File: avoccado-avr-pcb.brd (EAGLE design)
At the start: 17.8 x 33 mm, 29 parts, among them IC1 MCP1703CB, Q1 #MHz, Q2 MOSFET-NCHANNEL2N7002PW, U1 ATMEGA168#, U2 MCP73831, X1 Micro USB

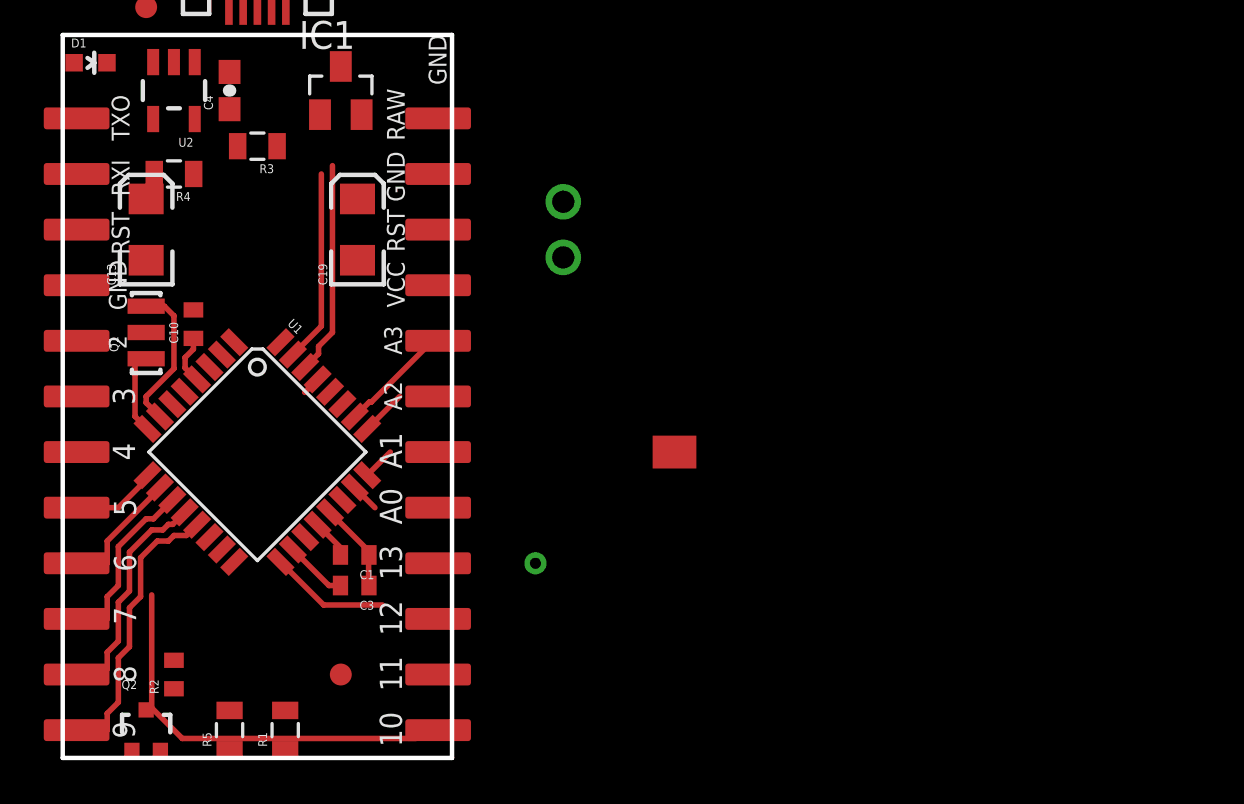
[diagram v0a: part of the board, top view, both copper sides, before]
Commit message: add NRF24 header wip
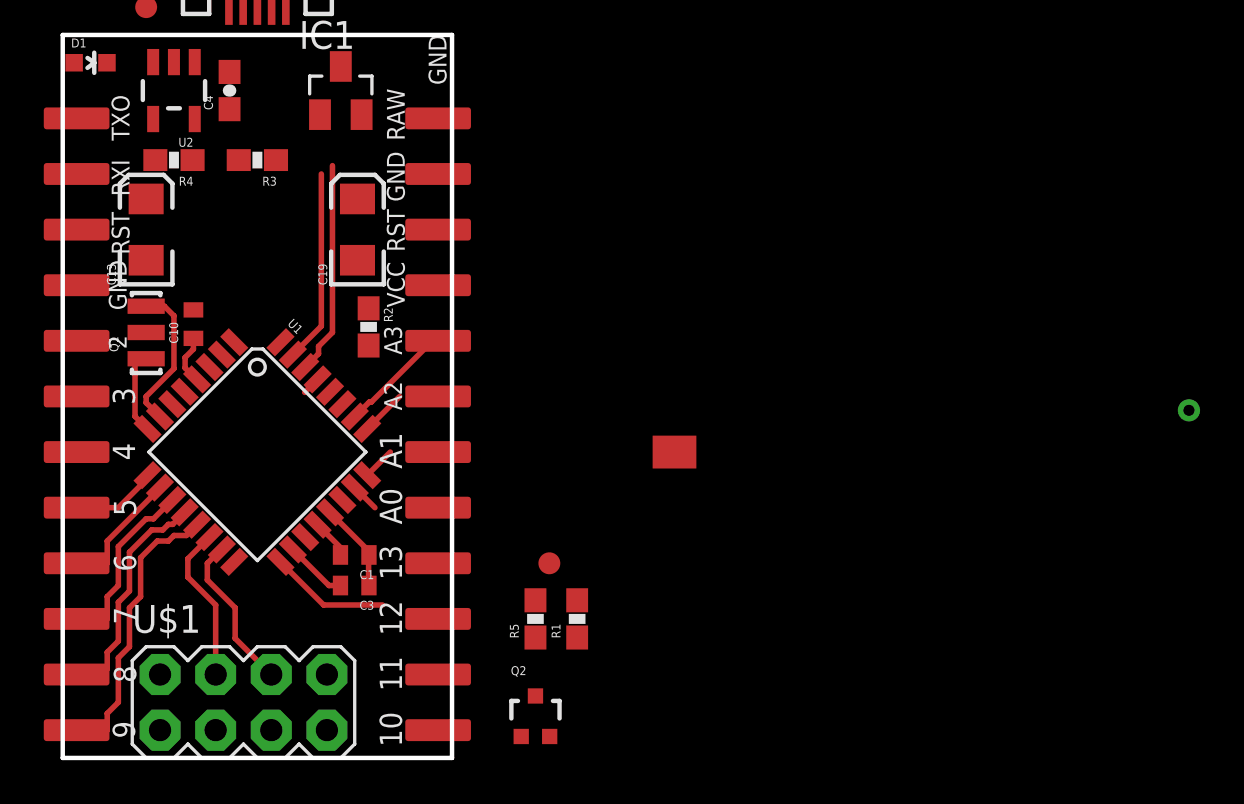
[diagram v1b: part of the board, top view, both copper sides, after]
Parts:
- removed JP2: (no value), SparkFun:1X02
- added U$1: M04X2, SparkFun-Connectors:2X4
- R1, R5: device SparkFun-Passives:0805 -> SparkFun-Resistors:0603-RES
- R2: device SparkFun:C0402 -> SparkFun-Resistors:0603-RES
- R3, R4: device SparkFun-Resistors:0805 -> SparkFun-Resistors:0603-RES
- moved R2 18.2 mm to (22.9, 31.1), turned to 270 degrees
- moved Q2 17.8 mm to (30.5, 13.3)
- moved R5 14.9 mm to (30.5, 17.8)
- moved R1 14.3 mm to (32.4, 17.8)
- moved U$2 10.8 mm to (31.1, 20.3)
- moved R3 0.63 mm to (17.8, 38.7)
- moved R4 0.63 mm to (14.0, 38.7)
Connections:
- new net 3.3V: U$1.2
- net A4: no longer JP2.1
- net A5: no longer JP2.2
- net D10: now also U$1.4
- net GND: now also U$1.1
- net MISO: now also U$1.7
- net MOSI: now also U$1.6
- net SCK: now also U$1.5
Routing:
- net D10: track 17.8 -> 7.21 mm
- net MOSI: track 0.00 -> 7.22 mm

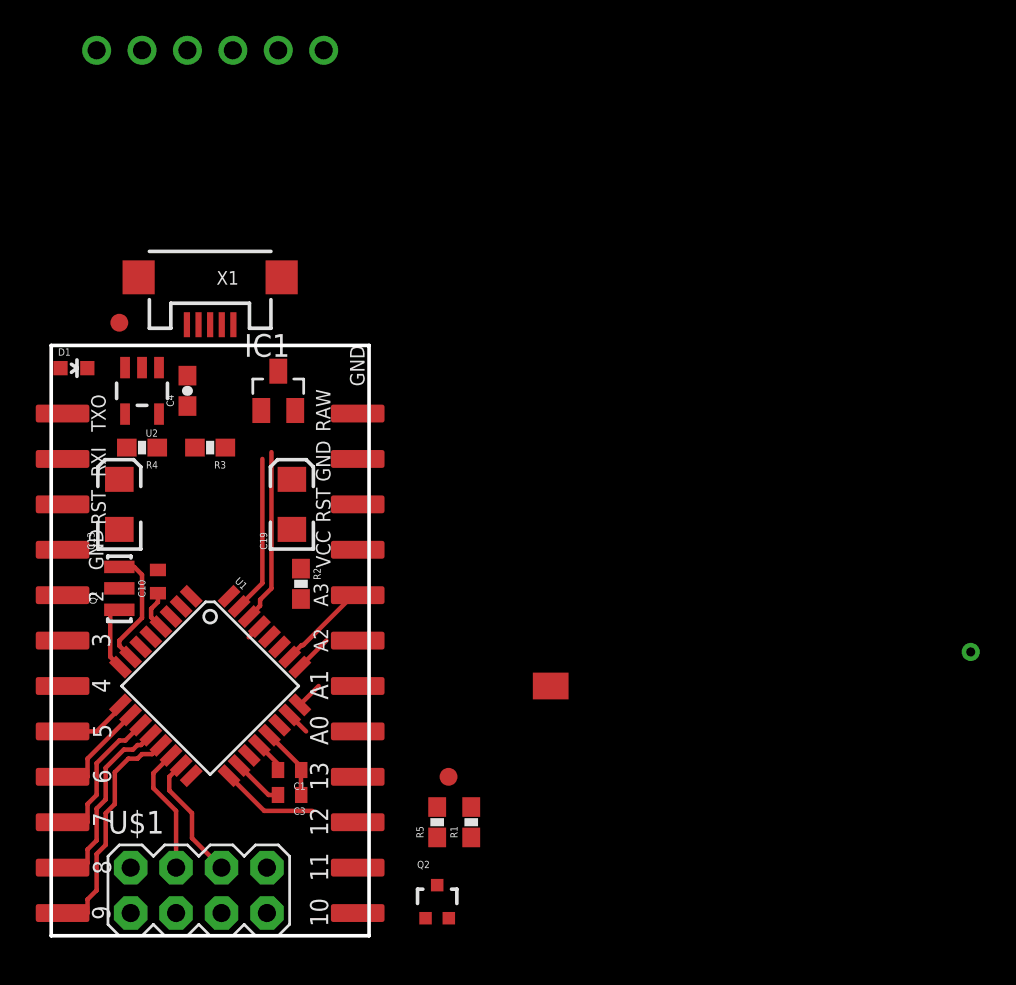
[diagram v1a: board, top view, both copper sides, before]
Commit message: reroute NRF24 header with bottom layer, add MPU6050 satellite board
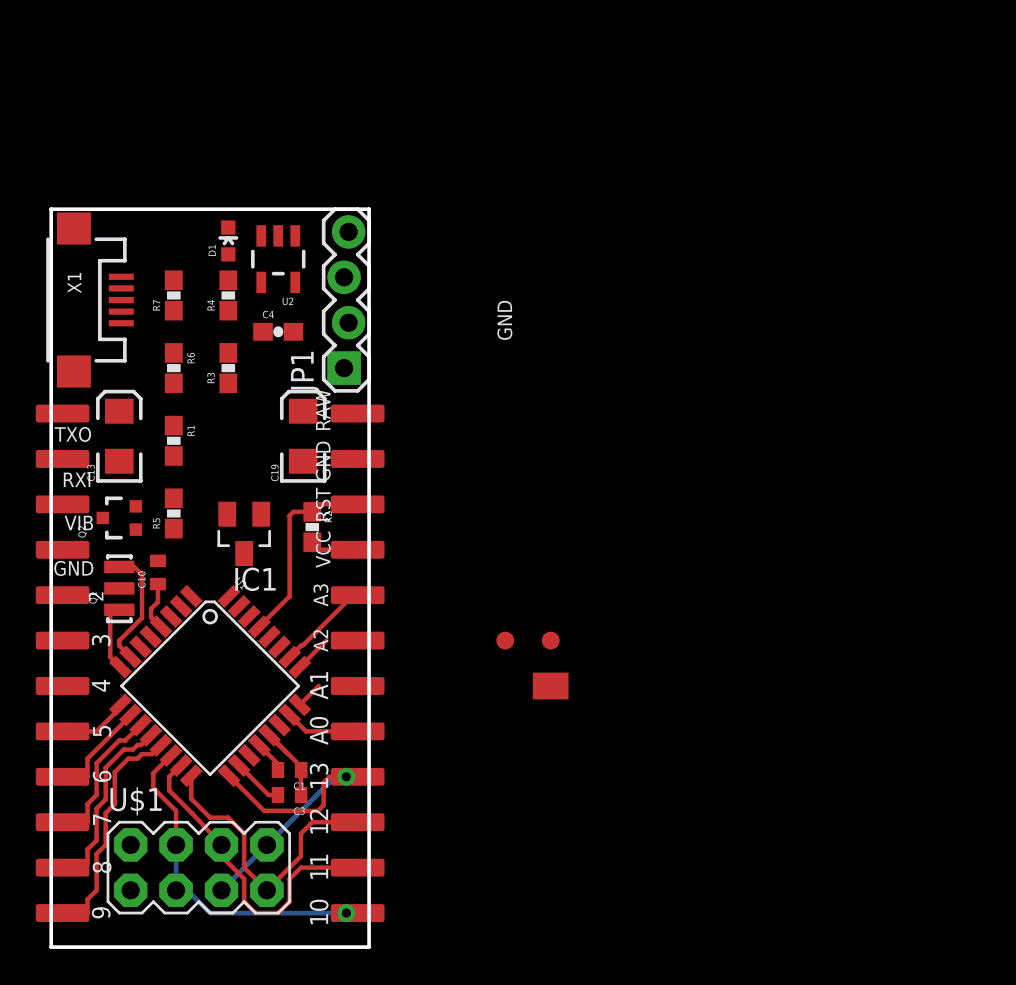
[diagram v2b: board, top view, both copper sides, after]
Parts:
- added R6, R7: 68, SparkFun-Resistors:0603-RES
- JP1: value FTDI Basic -> (none); device SparkFun:1X06 -> SparkFun-Connectors:1X04_LOCK
- moved U$4 30.0 mm to (36.8, 27.9)
- moved Q2 27.9 mm to (12.7, 34.8), turned to 90 degrees
- moved R1 27.1 mm to (15.7, 39.1), turned to 270 degrees
- moved R5 22.7 mm to (15.7, 35.1)
- moved JP1 22.6 mm to (25.4, 43.2), flipped to the top, turned to 90 degrees
- moved D1 11.2 mm to (18.8, 50.3), turned to 0 degrees
- moved U2 10.6 mm to (21.6, 49.3)
- moved R4 9.78 mm to (18.8, 47.2), turned to 90 degrees
- moved U$2 8.26 mm to (34.3, 27.9)
- moved IC1 8.22 mm to (19.7, 33.9), turned to 180 degrees
- moved X1 7.73 mm to (10.2, 47.0), turned to 270 degrees
- moved C4 6.06 mm to (21.6, 45.2), turned to 0 degrees
- moved R3 4.56 mm to (18.8, 43.2), turned to 90 degrees
- moved C19 3.86 mm to (23.0, 39.4)
- moved C13 3.81 mm to (12.7, 39.4)
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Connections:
- net RAW renamed BAT
- net VIN1 renamed BUS
- removed net DTR: JP1.1
- new net N$7: R7.1, X1.D+
- new net N$8: R6.1, X1.D-
- new net VIBR: JP11.2, Q2.3
- net A4: now also JP1.4
- net A5: now also JP1.3
- net D2: now also R7.2
- net D7: now also R6.2
- net GND: now also JP1.1; no longer JP1.5, JP1.6
- net RESET: no longer JP11.2
- net RXI: no longer JP1.3
- net TXO: no longer JP1.2
- net VCC: now also JP1.2; no longer JP1.4
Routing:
- net MISO: track 0.00 -> 16.2 mm
- net SCK: track 5.48 -> 19.2 mm, vias 0 -> 1
- net D10: track 7.21 -> 18.8 mm, vias 0 -> 1
- net MOSI: track 7.22 -> 18.0 mm
- net RESET: track 0.84 -> 11.0 mm
- net RXI: track 9.71 -> 0.00 mm
- net TXO: track 8.79 -> 0.00 mm
- net VCC: track 5.30 -> 8.39 mm
- net A0: track 1.30 -> 4.19 mm
- net GND: track 4.11 -> 4.96 mm, vias 1 -> 0
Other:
- board size 17.8 x 33 mm -> 17.8 x 41.3 mm
- board text added: "VIB"

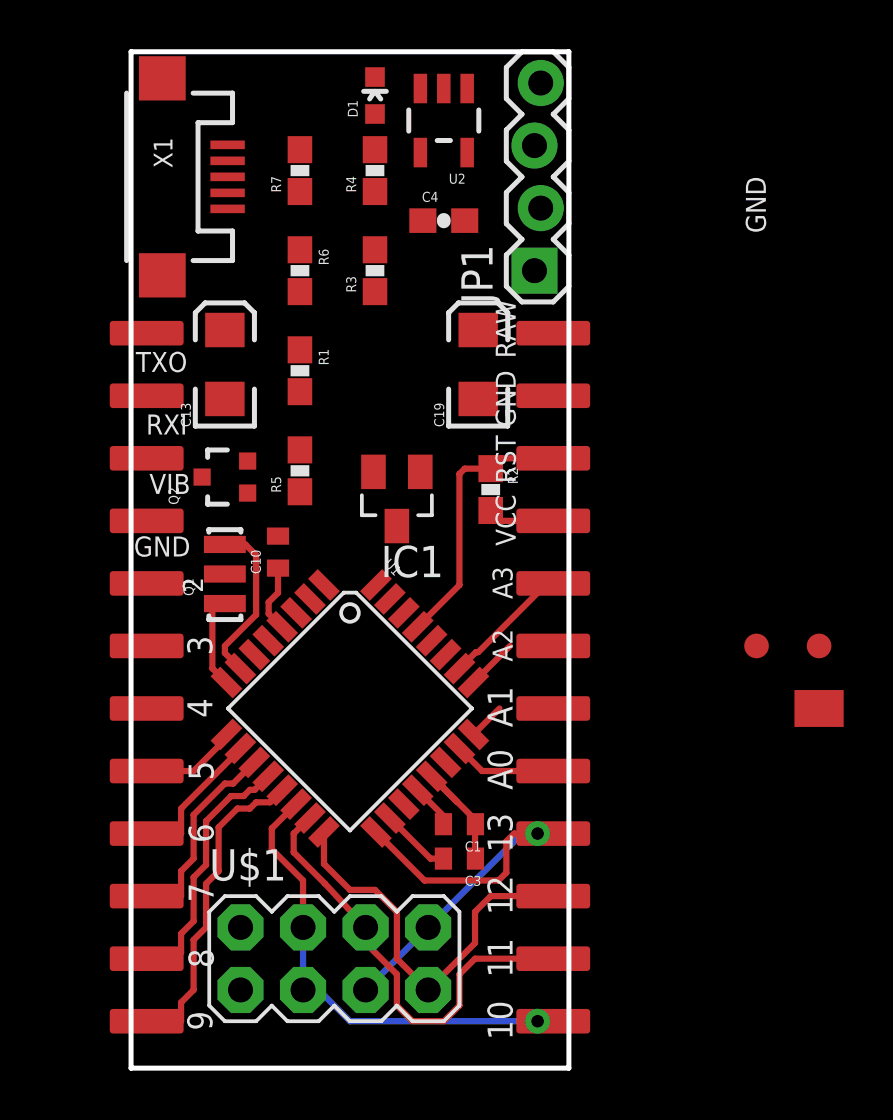
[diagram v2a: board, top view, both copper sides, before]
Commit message: route MPU6050 header
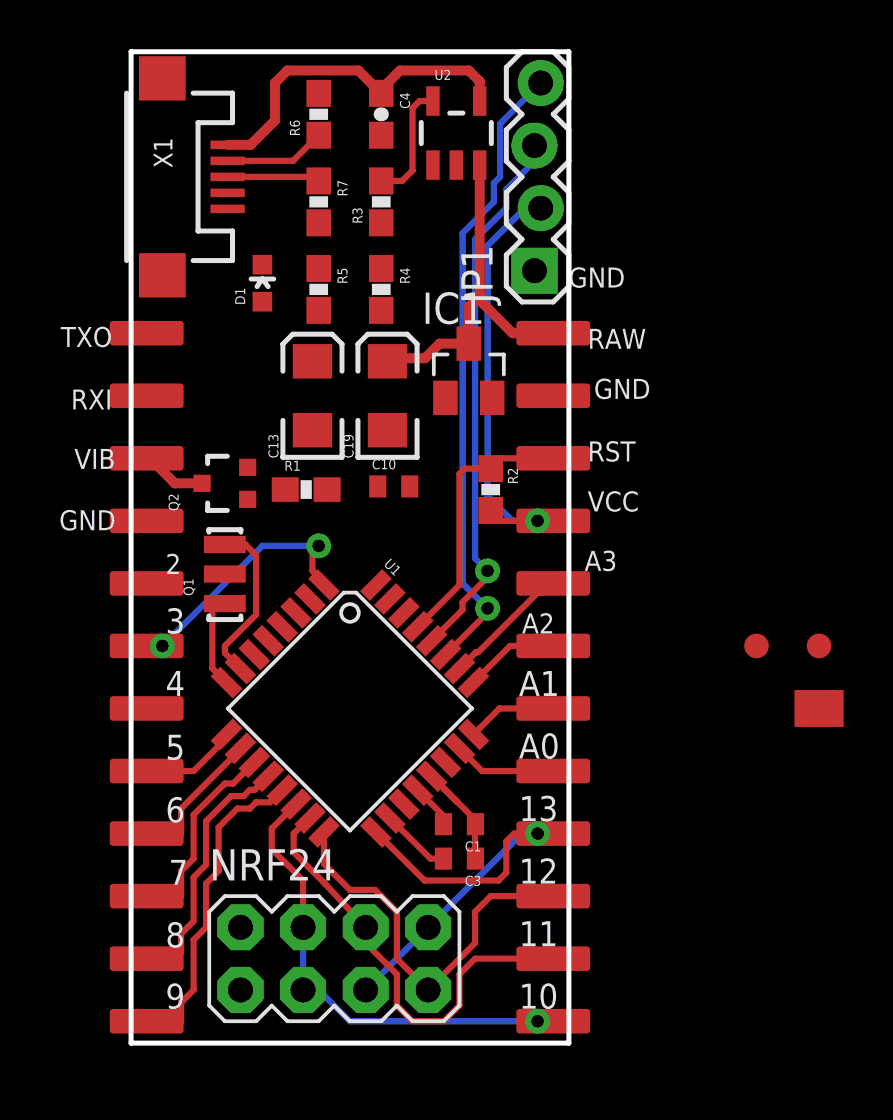
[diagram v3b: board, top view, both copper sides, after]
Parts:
- moved D1 8.89 mm to (14.2, 42.7)
- moved R5 7.41 mm to (16.5, 42.4), turned to 270 degrees
- moved R6 6.40 mm to (16.5, 49.5), turned to 90 degrees
- moved IC1 5.97 mm to (22.6, 39.1), turned to 0 degrees
- moved C10 5.40 mm to (19.6, 34.4), turned to 0 degrees
- moved C4 5.01 mm to (19.1, 49.5), turned to 270 degrees
- moved R1 4.83 mm to (16.0, 34.3), turned to 0 degrees
- moved R4 4.83 mm to (19.1, 42.4), turned to 270 degrees
- moved C19 3.90 mm to (19.3, 38.1)
- moved C13 3.78 mm to (16.3, 38.1)
- moved R3 2.81 mm to (19.1, 46.0)
- moved R7 1.48 mm to (16.5, 46.0), turned to 270 degrees
- moved U2 0.72 mm to (22.1, 48.8), turned to 0 degrees
- moved Q2 0.25 mm to (12.7, 34.5)
- renumbered U$1 to NRF24
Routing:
- net A4: track 0.00 -> 25.7 mm, vias 0 -> 1
- net A5: track 0.00 -> 22.3 mm, vias 0 -> 1
- net BAT: track 0.00 -> 14.8 mm
- net BUS: track 0.00 -> 14.2 mm
- net VCC: track 8.39 -> 21.0 mm, vias 0 -> 1
- net D3: track 0.00 -> 10.6 mm, vias 0 -> 2
- net N$3: track 0.00 -> 4.93 mm
- net N$8: track 0.00 -> 4.13 mm
- net N$7: track 0.00 -> 3.77 mm
- net VIBR: track 0.00 -> 2.67 mm
- net A1: track 1.49 -> 3.68 mm
- net A2: track 2.10 -> 3.85 mm
- net A3: track 4.45 -> 5.22 mm
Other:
- board size 17.8 x 41.3 mm -> 17.8 x 40.3 mm

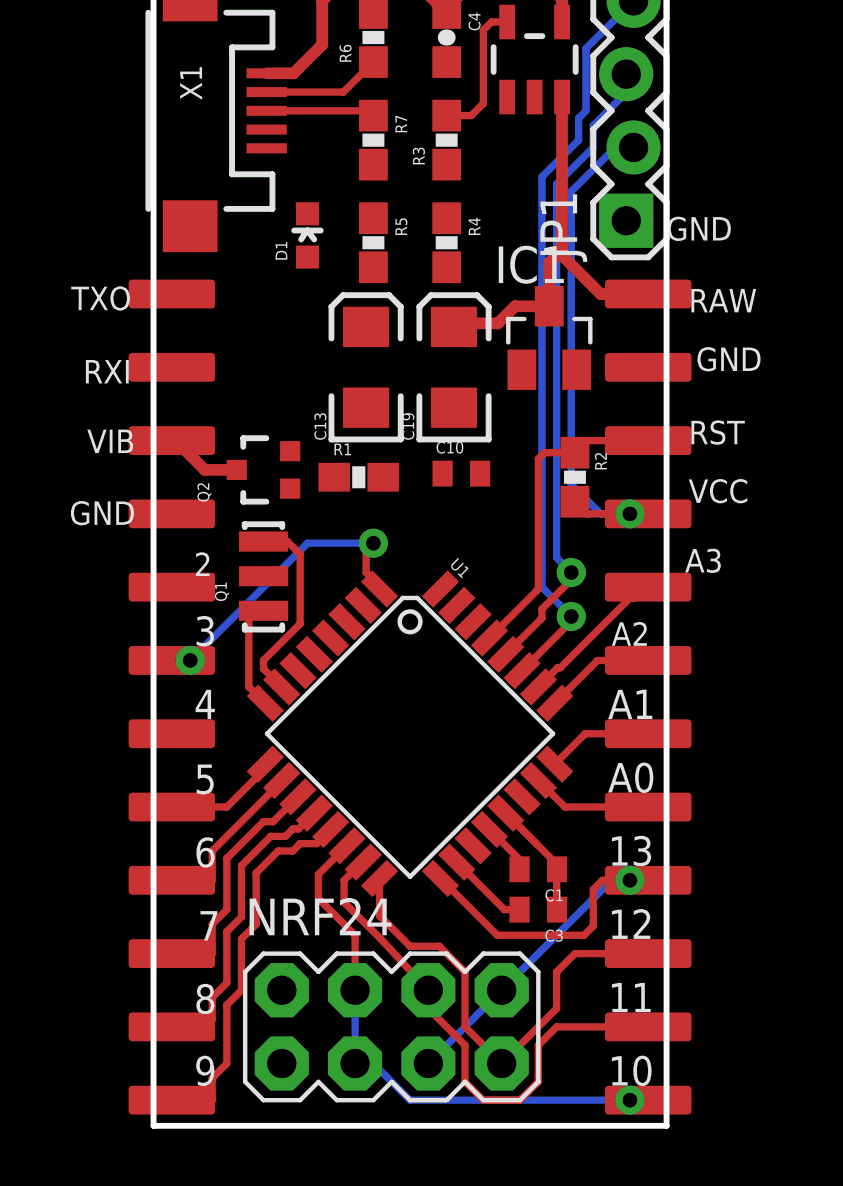
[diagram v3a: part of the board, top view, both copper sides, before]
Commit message: rewire filter caps
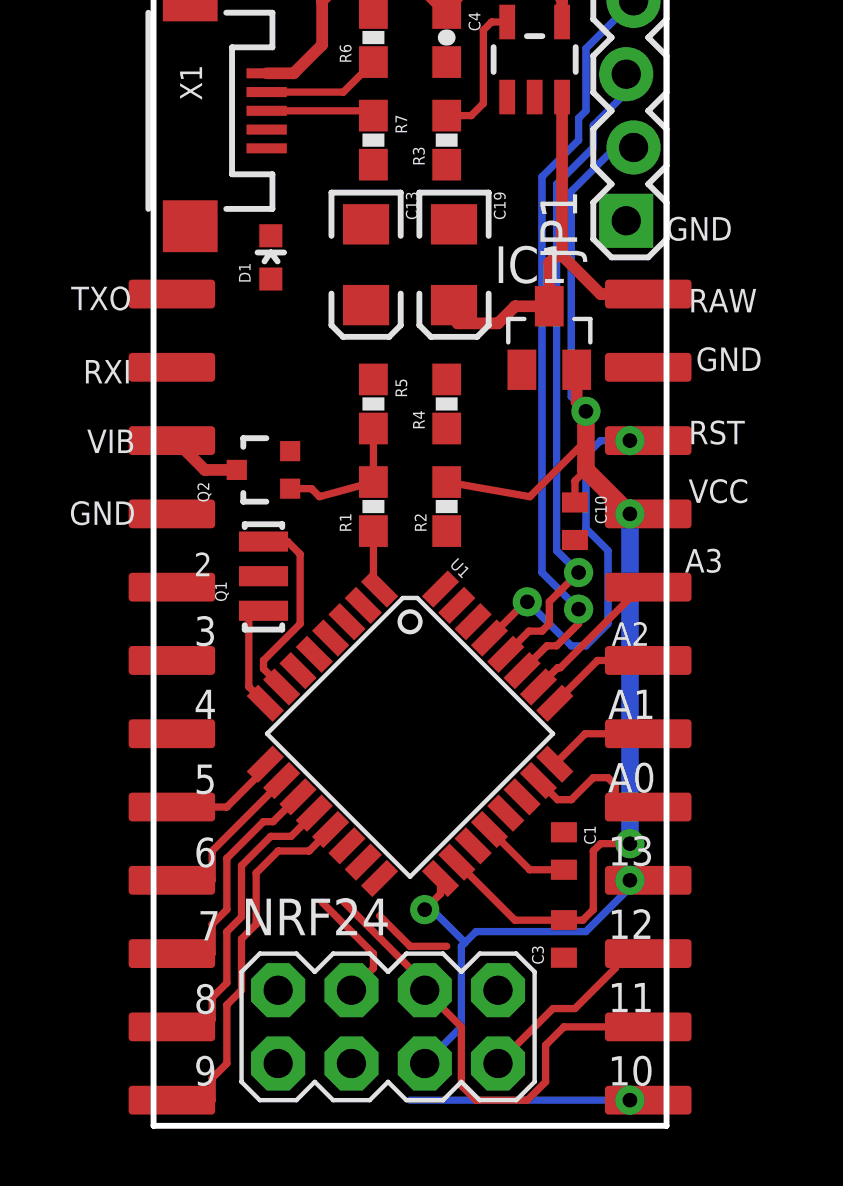
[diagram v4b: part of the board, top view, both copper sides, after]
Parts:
- moved R4 5.59 mm to (19.1, 36.8), turned to 90 degrees
- moved R5 5.59 mm to (16.5, 36.8)
- moved R2 4.56 mm to (19.1, 33.3), turned to 90 degrees
- moved C10 4.27 mm to (23.5, 32.8), turned to 270 degrees
- moved C13 3.56 mm to (16.3, 41.7), turned to 270 degrees
- moved C19 3.56 mm to (19.3, 41.7), turned to 270 degrees
- moved D1 1.48 mm to (13.0, 41.9)
- moved C3 1.35 mm to (23.1, 18.3), turned to 90 degrees
- moved R1 1.14 mm to (16.5, 33.3), turned to 90 degrees
- moved C1 1.09 mm to (23.1, 21.3), turned to 270 degrees
- moved NRF24 0.13 mm to (17.0, 15.2)
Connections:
- removed net D5-VIBR: JP10.1, R1.1, U1.9
- new net D5: JP10.1, U1.9
- net D3: now also R1.1
- net GND: now also D1.A; no longer R4.1
- net N$4: now also R4.2; no longer D1.C
- net N$5: now also D1.C, R4.1; no longer D1.A, R4.2
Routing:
- net VCC: track 21.0 -> 45.8 mm, vias 1 -> 3
- net D3: track 10.6 -> 2.10 mm, vias 2 -> 0
- net D10: track 18.8 -> 12.4 mm
- net MISO: track 16.2 -> 9.85 mm
- net GND: track 4.96 -> 0.00 mm
- net N$6: track 0.00 -> 4.92 mm
- net D5-VIBR: track 3.94 -> 0.00 mm
- net D5: track 0.00 -> 3.94 mm
- net SCK: track 19.2 -> 15.3 mm, vias 1 -> 2
- net RESET: track 11.0 -> 14.1 mm, vias 0 -> 2
- net MOSI: track 18.0 -> 16.6 mm
- net AREF: track 1.83 -> 3.16 mm
- net A0: track 4.19 -> 5.26 mm
